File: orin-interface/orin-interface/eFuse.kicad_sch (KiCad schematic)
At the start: 14 parts, among them U3 TPS259482AYWPR

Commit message: Finished: Orin-BoB
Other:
- note removed: "Fault- LED indicator"
- moved on the sheet: C10, C8, C9, D4, R13, R14, R15, R16, R18, U3

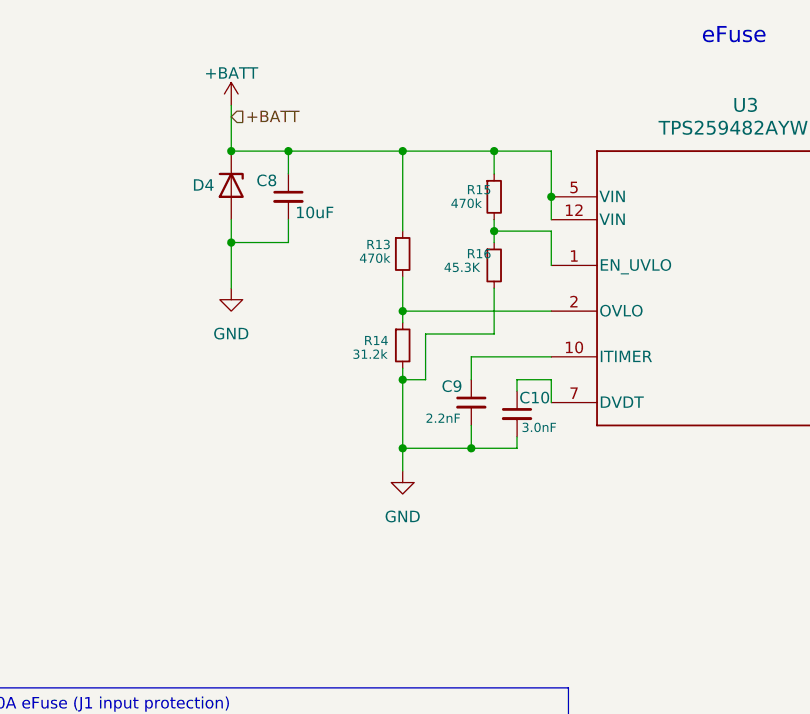
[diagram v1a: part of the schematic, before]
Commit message: orin-interface: PoE channels, buses, 3V3 regulator, ERC fixes
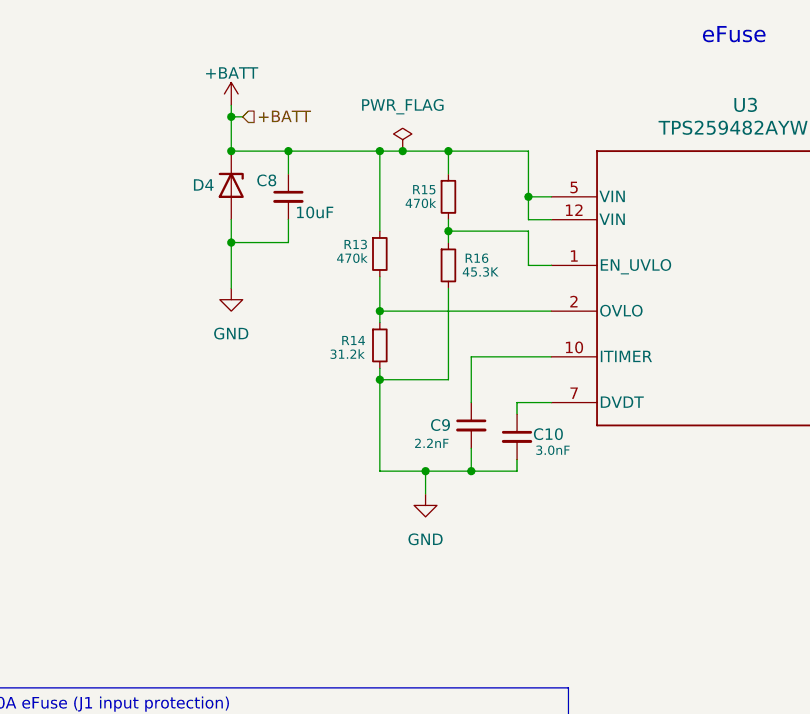
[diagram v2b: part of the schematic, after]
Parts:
- C10, C8, C9: footprint (none) -> Capacitor_SMD:C_0603_1608Metric_Pad1.08x0.95mm_HandSolder
- R13, R14, R15, R16, R17, R18, R19: footprint (none) -> Resistor_SMD:R_0603_1608Metric_Pad0.98x0.95mm_HandSolder
- U3: footprint YWP0012A-MFG -> TPS259482AYWPR:YWP0012A-MFG
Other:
- moved on the sheet: C10, C9, R13, R14, R15, R16

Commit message: orin-interface: add ETH connector sheets and Mate-connectors footprint lib; update orin-bob
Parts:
- removed D5: D_Zener, symbol Device:D_Zener
- removed D6: LED, symbol Device:LED
- removed R17: 4.7k, Resistor_SMD:R_0603_1608Metric_Pad0.98x0.95mm_HandSolder, symbol Device:R_Small
- added D1: 0603_150060RS75000, 150060RS75000:D_Wurth_WL-SMCW-0603, symbol 150060RS75000:0603_150060RS75000
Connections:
- net +BATT_P: now also R19.1
- net GND: now also D1.1 (-)
- net at R19.2: now also D1.2 (+)
- net FLT: no longer names the net of U3.4 (RCBCTRL)
- no-connect marks 1 -> 2
